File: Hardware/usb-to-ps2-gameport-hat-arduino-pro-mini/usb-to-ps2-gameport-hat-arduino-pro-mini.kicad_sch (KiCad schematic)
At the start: 27 parts, among them P1 Digital, P2 Analog

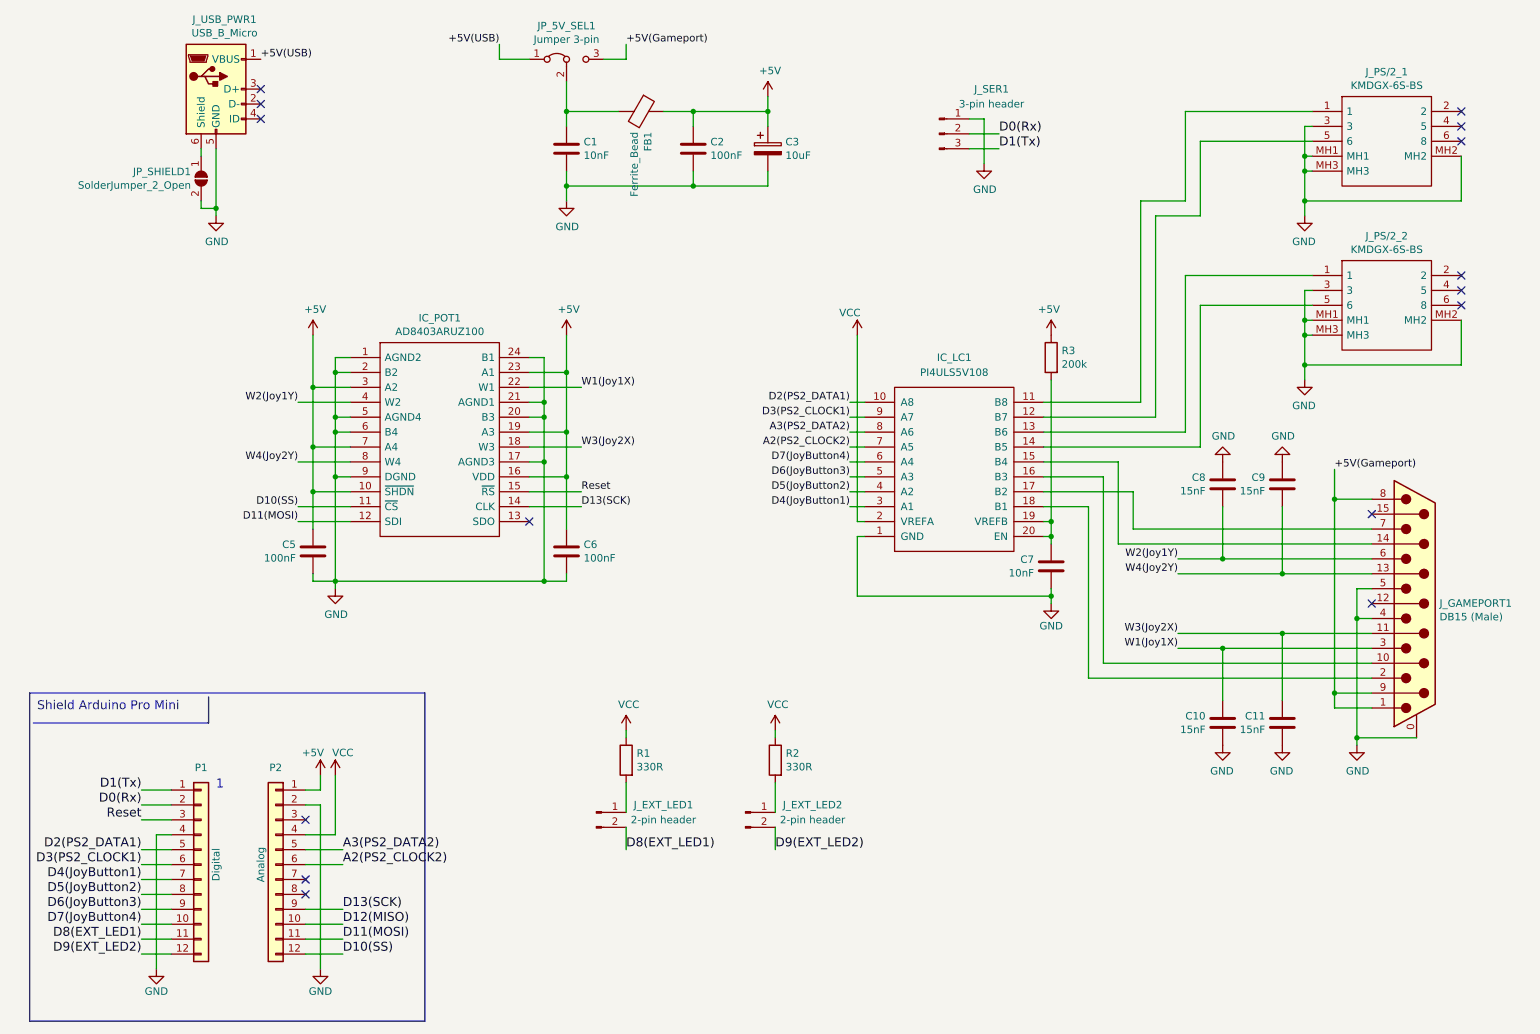
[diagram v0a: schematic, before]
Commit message: Merge PR#1 from @Ulfenknulfen
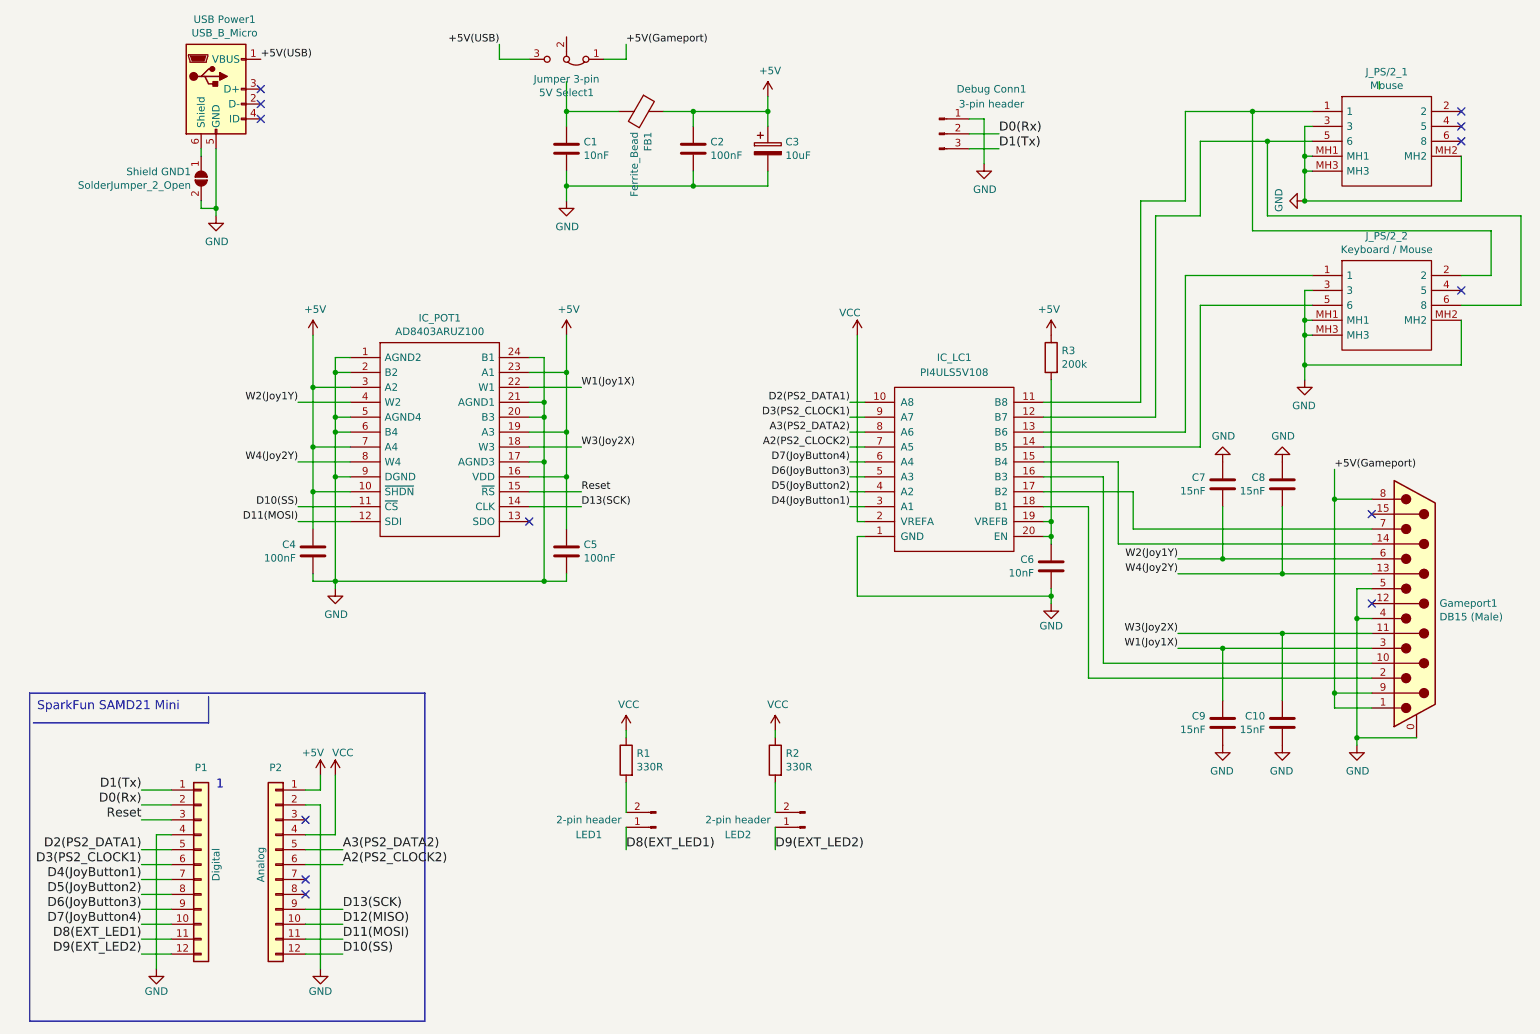
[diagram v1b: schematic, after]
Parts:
- 5V Select1: renamed from JP_5V_SEL1
- Debug Conn1: renamed from J_SER1
- J_PS/2_1: value KMDGX-6S-BS -> Mouse
- J_PS/2_2: value KMDGX-6S-BS -> Keyboard / Mouse
- Shield GND1: renamed from JP_SHIELD1
- USB Power1: renamed from J_USB_PWR1
- renumbered C11 to C10, C5 to C4, C6 to C5, C7 to C6, C8 to C7, C9 to C8, C10 to C9, J_GAMEPORT1 to Gameport1, J_EXT_LED1 to LED1, J_EXT_LED2 to LED2
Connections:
- net +5V(Gameport): now also 5V Select1.1 (A); no longer 5V Select1.3 (B)
- net +5V(USB): now also 5V Select1.3 (B); no longer 5V Select1.1 (A)
- net D8(EXT_LED1): now also LED1.1 (Pin_1); no longer LED1.2 (Pin_2)
- net D9(EXT_LED2): now also LED2.1 (Pin_1); no longer LED2.2 (Pin_2)
- net at C1.1, FB1.2: no longer 5V Select1.2 (C)
- net at IC_LC1.11 (B8), J_PS/2_1.1: now also J_PS/2_2.2
- net at IC_LC1.12 (B7), J_PS/2_1.5 (6): now also J_PS/2_2.6 (8)
- net at R1.2: now also LED1.2 (Pin_2); no longer LED1.1 (Pin_1)
- net at R2.2: now also LED2.2 (Pin_2); no longer LED2.1 (Pin_1)
- no-connect marks 15 -> 13
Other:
- note added: "SparkFun SAMD21 Mini"
- note removed: "Shield Arduino Pro Mini"
- company: © 2019 by Deadman -> © 2024 by Deadman
- moved on the sheet: 5V Select1, LED1, LED2

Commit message: @Ulfenknulfen: connect base of digi-pot with wiper
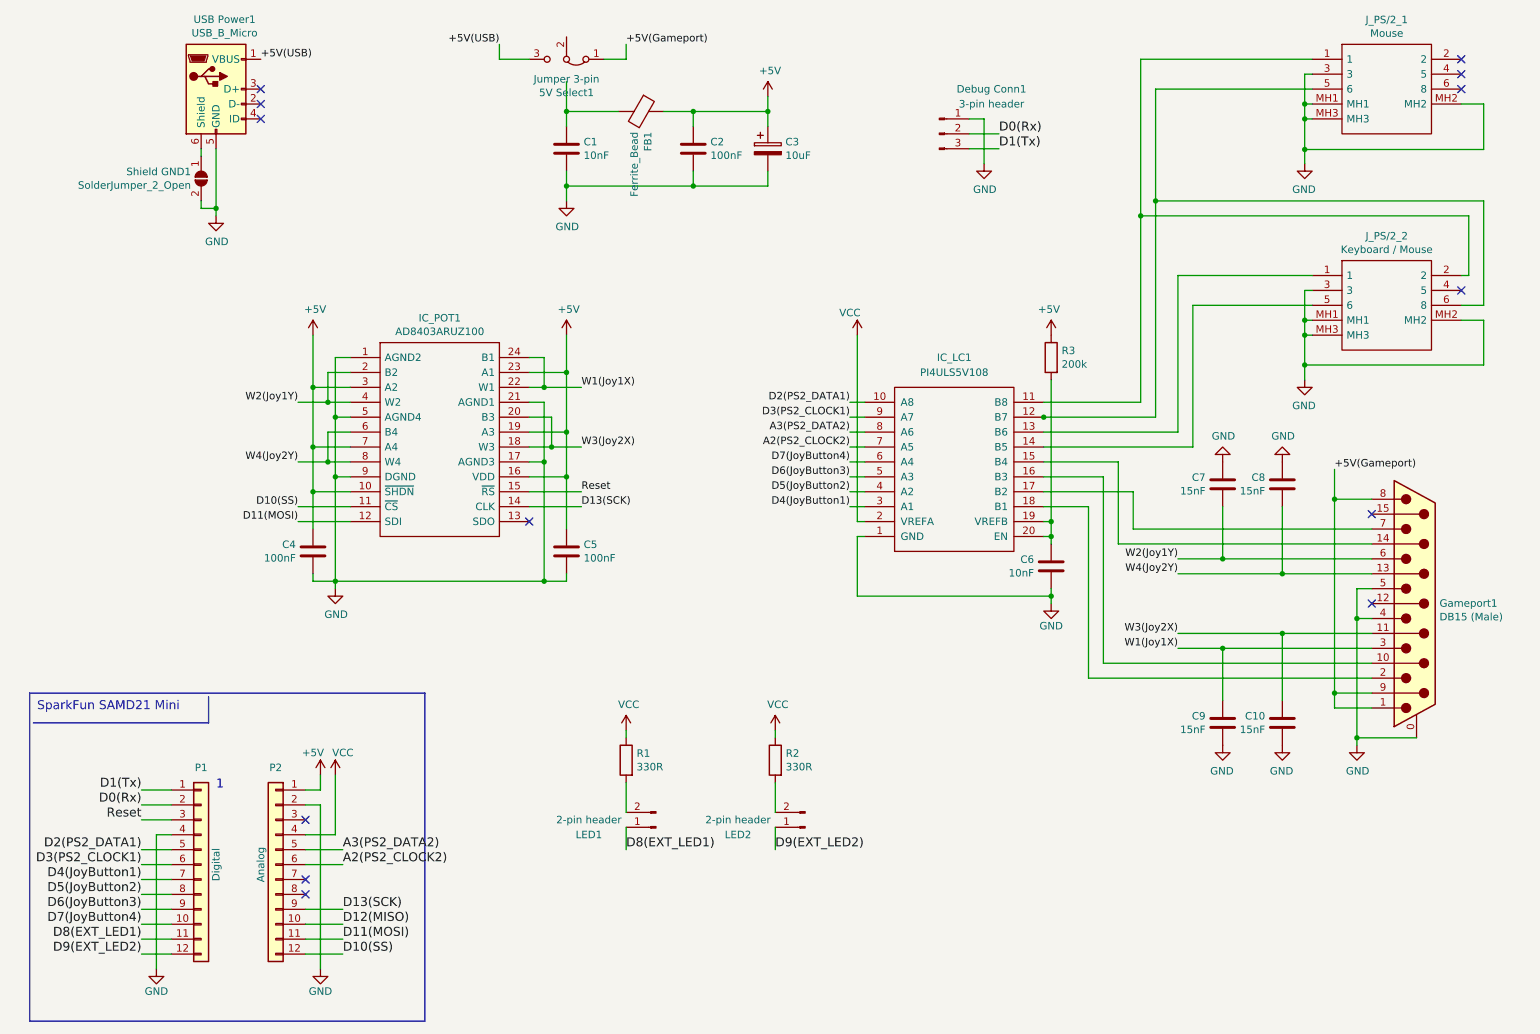
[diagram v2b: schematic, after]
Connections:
- net GND: no longer IC_POT1.2 (B2), IC_POT1.20 (B3), IC_POT1.24 (B1), IC_POT1.6 (B4)
- net W1(Joy1X): now also IC_POT1.24 (B1)
- net W2(Joy1Y): now also IC_POT1.2 (B2)
- net W3(Joy2X): now also IC_POT1.20 (B3)
- net W4(Joy2Y): now also IC_POT1.6 (B4)
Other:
- company: © 2024 by Deadman -> © 2019 by Deadman
- moved on the sheet: J_PS/2_1

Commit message: prepare Release V1.4
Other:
- company: © 2019 by Deadman -> © 2024 by Deadman
- moved on the sheet: P1, P2
